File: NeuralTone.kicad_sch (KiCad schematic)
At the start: 84 parts, among them J1 Power Port (5V@3A), J2 Guitar, J3 Headphone, J4 USB Port, J5 Line Out, J6 TF-01A, SW1 SW_Push, U1 MCP6022, U2 LDLN025M33R, U3 LDLN025M33R, U4 AP2151, U5 NAU8814YG, U6 USBLC6-2P6, Y1 DSB211SDN 26MHz

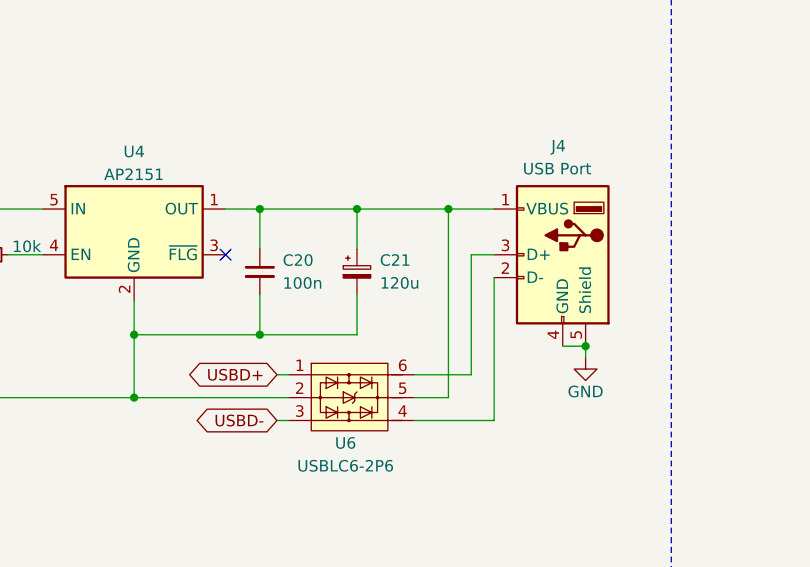
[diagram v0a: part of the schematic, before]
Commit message: change current limiter cap
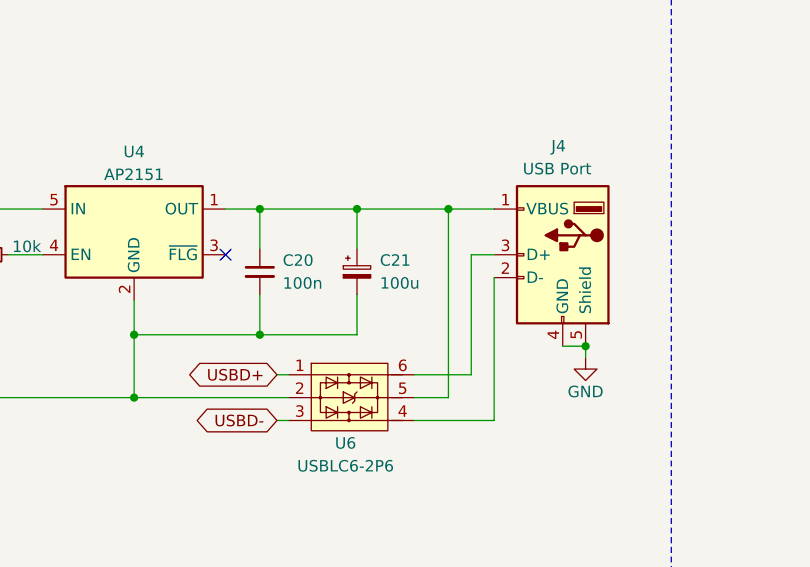
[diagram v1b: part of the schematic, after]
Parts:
- C21: value 120u -> 100u
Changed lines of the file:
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@@
       (effects (font (size 1.27 1.27)) (justify left))
     )
-    (property "Value" "120u" (at 360.045 53.975 0)
+    (property "Value" "100u" (at 360.045 53.975 0)
       (effects (font (size 1.27 1.27)) (justify left))
     )

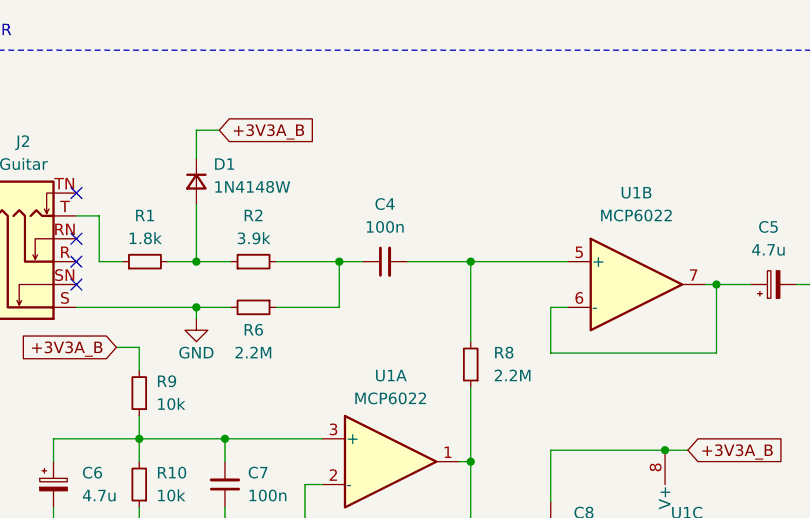
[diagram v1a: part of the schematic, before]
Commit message: change audio signal film cap to something more available
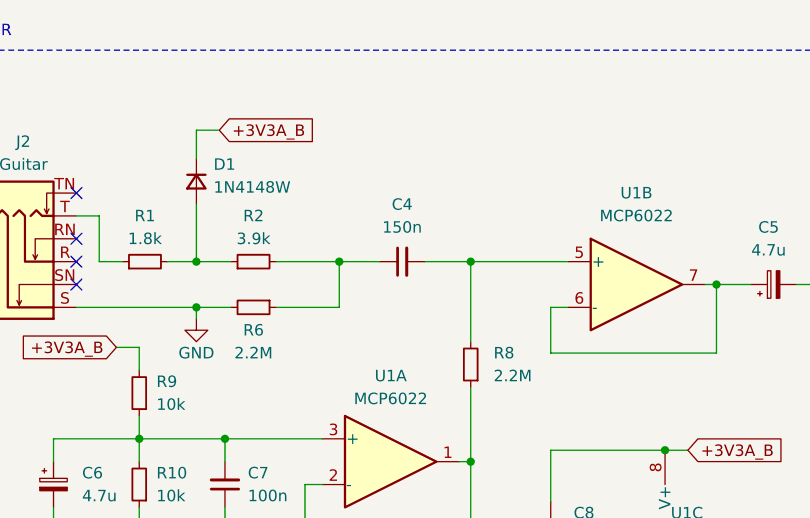
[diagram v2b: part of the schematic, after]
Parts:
- C4: value 100n -> 150n; footprint Capacitor_SMD:C_0805_2012Metric_Pad1.18x1.45mm_HandSolder -> Capacitor_SMD:C_1206_3216Metric_Pad1.33x1.80mm_HandSolder
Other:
- moved on the sheet: C4
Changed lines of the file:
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@@
   (junction (at 229.87 128.905) (diameter 0) (color 0 0 0 0)
   )
-  (junction (at 208.28 43.815) (diameter 0) (color 0 0 0 0)
-  )
   (junction (at 90.17 135.255) (diameter 0) (color 0 0 0 0)
   )
@@
   (junction (at 367.665 45.72) (diameter 0) (color 0 0 0 0)
   )
+  (junction (at 208.28 43.815) (diameter 0) (color 0 0 0 0)
+  )
   (junction (at 90.17 145.415) (diameter 0) (color 0 0 0 0)
   )
@@
     (stroke (width 0) (type default))
   )
-  (wire (pts (xy 201.295 43.815) (xy 208.28 43.815))
-    (stroke (width 0) (type default))
-  )
   (wire (pts (xy 227.33 153.67) (xy 229.87 153.67))
     (stroke (width 0) (type default))
@@
     (stroke (width 0) (type default))
   )
-  (wire (pts (xy 193.675 43.815) (xy 196.215 43.815))
+  (wire (pts (xy 193.675 43.815) (xy 198.12 43.815))
     (stroke (width 0) (type default))
   )
@@
     (stroke (width 0) (type default))
   )
+  (wire (pts (xy 203.2 43.815) (xy 208.28 43.815))
+    (stroke (width 0) (type default))
+  )
   (wire (pts (xy 55.245 213.36) (xy 79.375 213.36))
     (stroke (width 0) (type default))
@@
     )
   )
-  (symbol (lib_id "Device:C_Small") (at 198.755 43.815 90) (unit 1)
+  (symbol (lib_id "Device:C_Small") (at 200.66 43.815 90) (unit 1)
     (in_bom yes) (on_board yes) (dnp no) (fields_autoplaced)
-    (property "Reference" "C4" (at 198.7613 37.465 90)
+    (property "Reference" "C4" (at 200.6663 37.465 90)
       (effects (font (size 1.27 1.27)))
     )
-    (property "Value" "100n" (at 198.7613 40.005 90)
+    (property "Value" "150n" (at 200.6663 40.005 90)
       (effects (font (size 1.27 1.27)))
     )
-    (property "Footprint" "Capacitor_SMD:C_0805_2012Metric_Pad1.18x1.45mm_HandSolder" (at 198.755 43.815 0)
+    (property "Footprint" "Capacitor_SMD:C_1206_3216Metric_Pad1.33x1.80mm_HandSolder" (at 200.66 43.815 0)
       (effects (font (size 1.27 1.27)) hide)
     )
-    (property "Datasheet" "~" (at 198.755 43.815 0)
+    (property "Datasheet" "~" (at 200.66 43.815 0)
       (effects (font (size 1.27 1.27)) hide)
     )

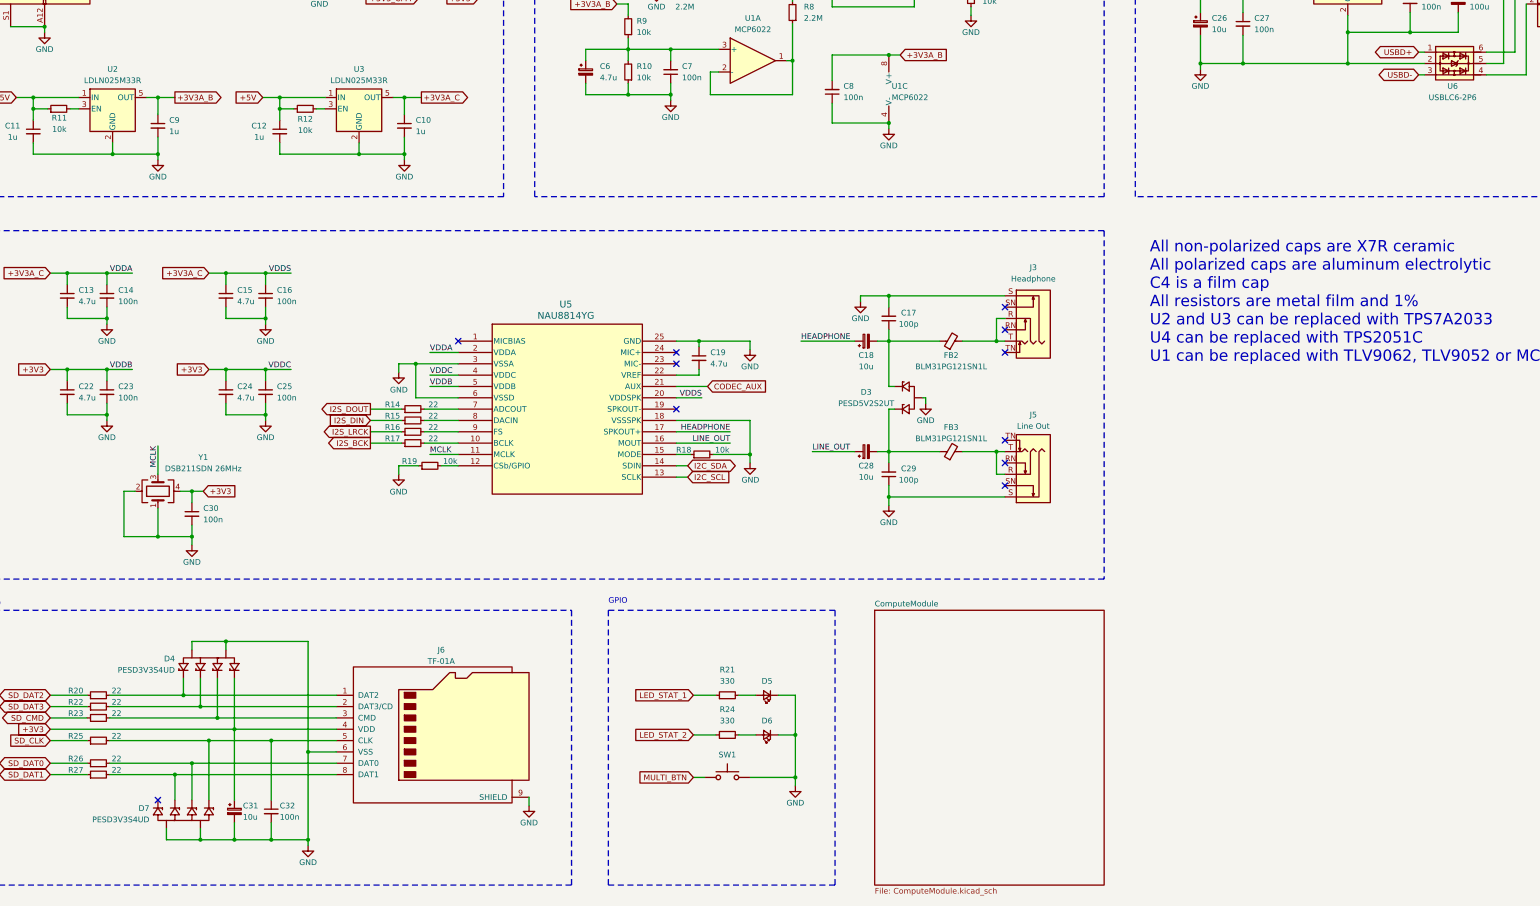
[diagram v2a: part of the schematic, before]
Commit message: rename TVS IC to D
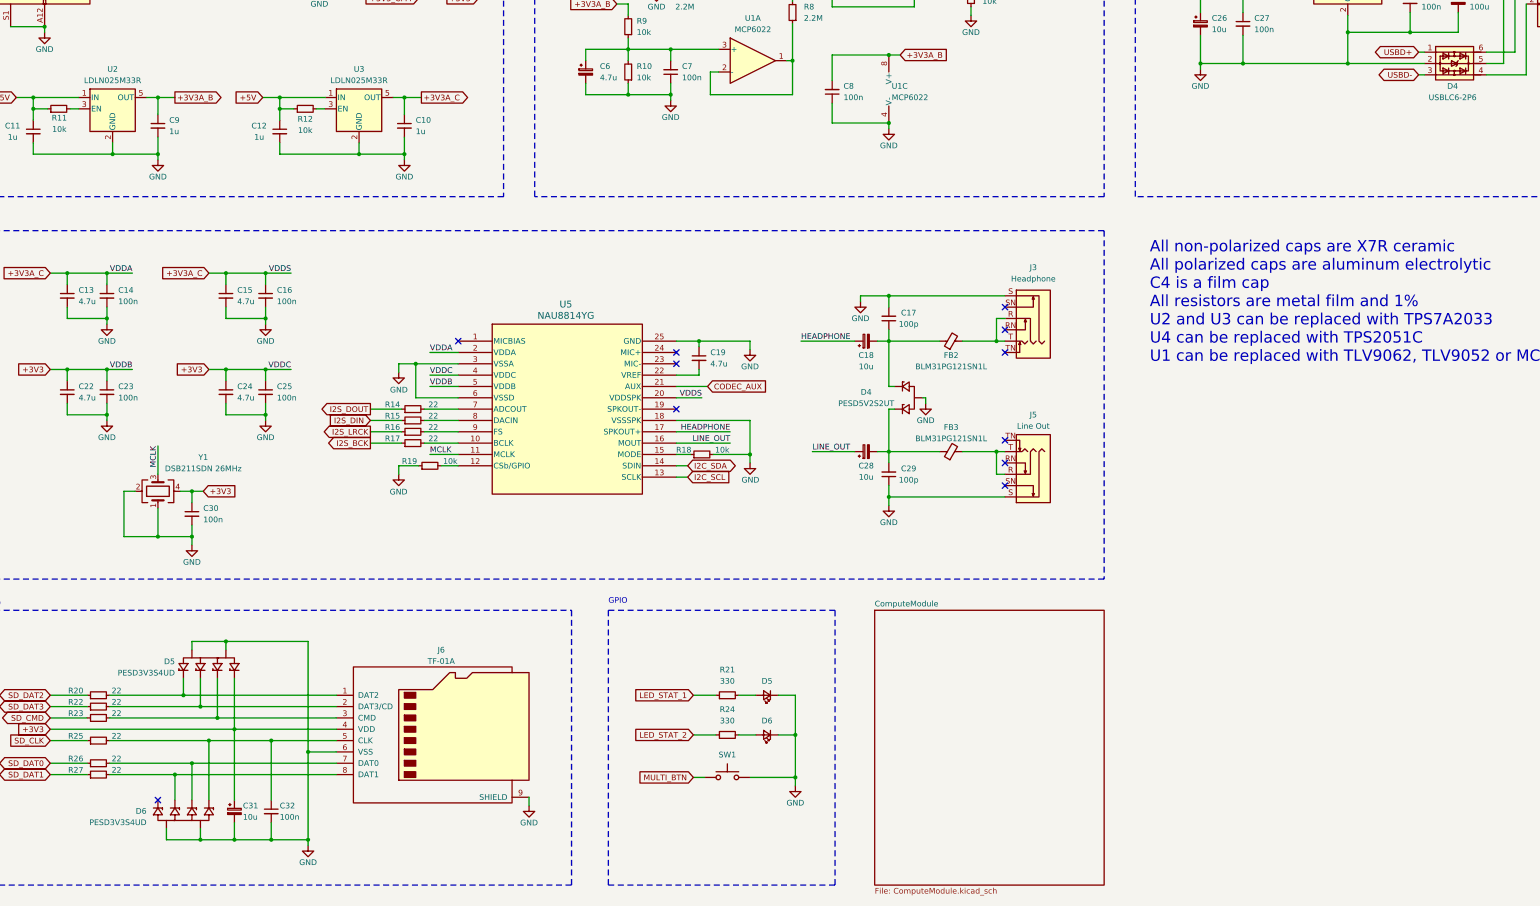
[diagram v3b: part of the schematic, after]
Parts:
- renumbered U6 to D4, D3 to D4, D4 to D5, D7 to D6
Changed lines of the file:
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@@
   (symbol (lib_id "NeuralTone:USBLC6-2P6") (at 357.505 66.675 0) (unit 1)
     (in_bom yes) (on_board yes) (dnp no)
-    (property "Reference" "U6" (at 356.235 71.755 0)
+    (property "Reference" "D4" (at 356.235 71.755 0)
       (effects (font (size 1.27 1.27)))
     )
@@
       (project "NeuralTone"
         (path "/ac6c2b5b-00d5-42f9-9826-f03f3806195c"
-          (reference "U6") (unit 1)
+          (reference "D4") (unit 1)
         )
       )
@@
   (symbol (lib_id "NeuralTone:D_TVS_Quad") (at 77.47 201.93 90) (unit 1)
     (in_bom yes) (on_board yes) (dnp no) (fields_autoplaced)
-    (property "Reference" "D4" (at 69.85 200.0885 90)
-      (effects (font (size 1.27 1.27)) (justify left))
-    )
-    (property "Value" "PESD3V3S4UD" (at 69.85 202.6285 90)
+    (property "Reference" "D5" (at 69.85 200.7235 90)
+      (effects (font (size 1.27 1.27)) (justify left))
+    )
+    (property "Value" "PESD3V3S4UD" (at 69.85 203.2635 90)
       (effects (font (size 1.27 1.27)) (justify left))
     )
@@
       (project "NeuralTone"
         (path "/ac6c2b5b-00d5-42f9-9826-f03f3806195c"
-          (reference "D4") (unit 1)
+          (reference "D5") (unit 1)
         )
       )
@@
   (symbol (lib_id "NeuralTone:D_TVS_Dual") (at 233.68 141.605 0) (unit 1)
     (in_bom yes) (on_board yes) (dnp no)
-    (property "Reference" "D3" (at 224.79 140.335 0)
+    (property "Reference" "D4" (at 224.79 140.335 0)
       (effects (font (size 1.27 1.27)))
     )
@@
       (project "NeuralTone"
         (path "/ac6c2b5b-00d5-42f9-9826-f03f3806195c"
-          (reference "D3") (unit 1)
+          (reference "D4") (unit 1)
         )
       )
@@
   (symbol (lib_id "NeuralTone:D_TVS_Quad") (at 71.755 234.315 270) (unit 1)
     (in_bom yes) (on_board yes) (dnp no) (fields_autoplaced)
-    (property "Reference" "D7" (at 64.135 233.6165 90)
+    (property "Reference" "D6" (at 63.5 234.2515 90)
       (effects (font (size 1.27 1.27)) (justify right))
     )
-    (property "Value" "PESD3V3S4UD" (at 64.135 236.1565 90)
+    (property "Value" "PESD3V3S4UD" (at 63.5 236.7915 90)
       (effects (font (size 1.27 1.27)) (justify right))
     )
@@
       (project "NeuralTone"
         (path "/ac6c2b5b-00d5-42f9-9826-f03f3806195c"
-          (reference "D7") (unit 1)
-        )
-      )
+          (reference "D6") (unit 1)
+        )
+      )

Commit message: fix diode number
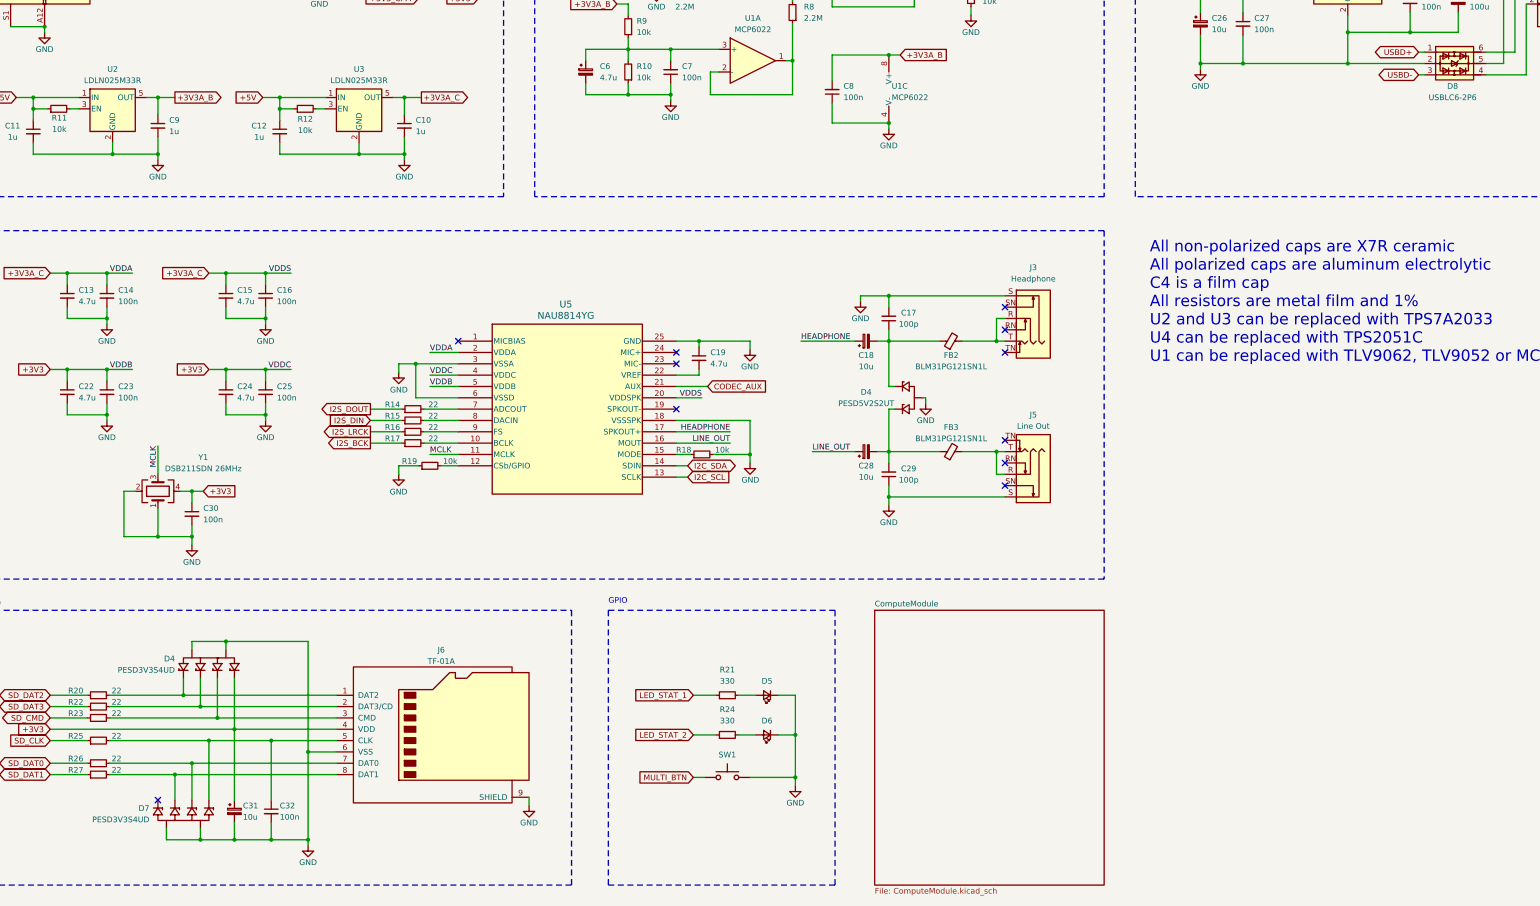
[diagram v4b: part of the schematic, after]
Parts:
- renumbered D5 to D4, D6 to D7, D4 to D8
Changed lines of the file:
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@@
   (symbol (lib_id "NeuralTone:USBLC6-2P6") (at 357.505 66.675 0) (unit 1)
     (in_bom yes) (on_board yes) (dnp no)
-    (property "Reference" "D4" (at 356.235 71.755 0)
+    (property "Reference" "D8" (at 356.235 71.755 0)
       (effects (font (size 1.27 1.27)))
     )
@@
       (project "NeuralTone"
         (path "/ac6c2b5b-00d5-42f9-9826-f03f3806195c"
-          (reference "D4") (unit 1)
+          (reference "D8") (unit 1)
         )
       )
@@
   (symbol (lib_id "NeuralTone:D_TVS_Quad") (at 77.47 201.93 90) (unit 1)
     (in_bom yes) (on_board yes) (dnp no) (fields_autoplaced)
-    (property "Reference" "D5" (at 69.85 200.7235 90)
-      (effects (font (size 1.27 1.27)) (justify left))
-    )
-    (property "Value" "PESD3V3S4UD" (at 69.85 203.2635 90)
+    (property "Reference" "D4" (at 69.85 200.0885 90)
+      (effects (font (size 1.27 1.27)) (justify left))
+    )
+    (property "Value" "PESD3V3S4UD" (at 69.85 202.6285 90)
       (effects (font (size 1.27 1.27)) (justify left))
     )
@@
       (project "NeuralTone"
         (path "/ac6c2b5b-00d5-42f9-9826-f03f3806195c"
-          (reference "D5") (unit 1)
+          (reference "D4") (unit 1)
         )
       )
@@
   (symbol (lib_id "NeuralTone:D_TVS_Quad") (at 71.755 234.315 270) (unit 1)
     (in_bom yes) (on_board yes) (dnp no) (fields_autoplaced)
-    (property "Reference" "D6" (at 63.5 234.2515 90)
+    (property "Reference" "D7" (at 64.135 233.6165 90)
       (effects (font (size 1.27 1.27)) (justify right))
     )
-    (property "Value" "PESD3V3S4UD" (at 63.5 236.7915 90)
+    (property "Value" "PESD3V3S4UD" (at 64.135 236.1565 90)
       (effects (font (size 1.27 1.27)) (justify right))
     )
@@
       (project "NeuralTone"
         (path "/ac6c2b5b-00d5-42f9-9826-f03f3806195c"
-          (reference "D6") (unit 1)
-        )
-      )
+          (reference "D7") (unit 1)
+        )
+      )

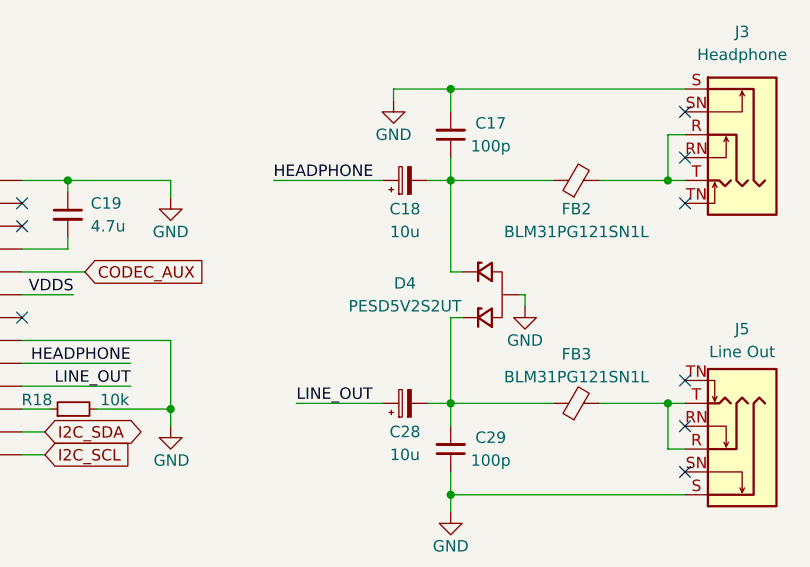
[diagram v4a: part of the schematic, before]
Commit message: fix diode number
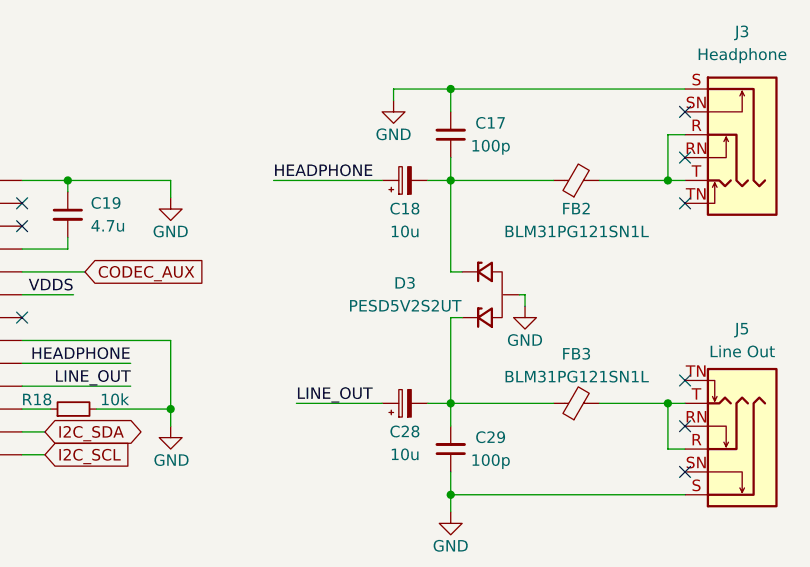
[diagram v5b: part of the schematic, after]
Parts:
- renumbered D4 to D3
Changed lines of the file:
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@@
   (symbol (lib_id "NeuralTone:D_TVS_Dual") (at 233.68 141.605 0) (unit 1)
     (in_bom yes) (on_board yes) (dnp no)
-    (property "Reference" "D4" (at 224.79 140.335 0)
+    (property "Reference" "D3" (at 224.79 140.335 0)
       (effects (font (size 1.27 1.27)))
     )
@@
       (project "NeuralTone"
         (path "/ac6c2b5b-00d5-42f9-9826-f03f3806195c"
-          (reference "D4") (unit 1)
+          (reference "D3") (unit 1)
         )
       )

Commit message: initial 3D files and pcb
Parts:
- D3: footprint Package_TO_SOT_SMD:SOT-23_Handsoldering -> Package_TO_SOT_SMD:SOT-23
- SW1: footprint Button_Switch_SMD:SW_DIP_SPSTx01_Slide_6.7x4.1mm_W6.73mm_P2.54mm_LowProfile_JPin -> Button_Switch_SMD:SW_SPST_Omron_B3FS-105xP
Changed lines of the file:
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@@
       (effects (font (size 1.27 1.27)))
     )
-    (property "Footprint" "Package_TO_SOT_SMD:SOT-23_Handsoldering" (at 233.68 144.145 90)
+    (property "Footprint" "Package_TO_SOT_SMD:SOT-23" (at 233.68 144.145 90)
       (effects (font (size 1.27 1.27)) hide)
     )
@@
       (effects (font (size 1.27 1.27)) hide)
     )
-    (property "Footprint" "Button_Switch_SMD:SW_DIP_SPSTx01_Slide_6.7x4.1mm_W6.73mm_P2.54mm_LowProfile_JPin" (at 193.675 221.615 0)
-      (effects (font (size 1.27 1.27)) hide)
-    )
+    (property "Footprint" "Button_Switch_SMD:SW_SPST_Omron_B3FS-105xP" (at 193.675 221.615 0)
+      (effects (font (size 1.27 1.27)) hide)
+    )
